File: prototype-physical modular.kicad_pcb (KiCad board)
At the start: 2 copper layers, 100 x 164 mm, 187 parts, among them CON1 BARREL_JACK, CON2 SD_Card, IC1 ATMEGA2560-A, P1 POWER, P10 PC, P11 CONN_UART, P12 PJ, P13 PD, P14 PE, P15 PH, P16 PF, P17 SD_PINS, P18 3VI2C, P19 PIGPIO, P2 FTDI, P20 MIDI_IN, P21 MIDI_OUT, P22 BUSTI, P23 BUSTO, P3 SPI, P7 PA, P8 PL, P9 PB, Q1 BSS138, Q2 BSS138, Q3 BSS138, Q4 BSS138, Q5 BSS138, Q6 BSS138, SW1 SW_PUSH, SW10 SW_PUSH, SW11 SW_PUSH, SW12 SW_PUSH, SW13 SW_PUSH, SW14 SW_PUSH, SW2 ROTARY_ENCODER_SWITCH, SW3 SW_PUSH, SW4 SW_PUSH, SW5 SW_PUSH, SW6 SW_PUSH, SW7 SW_PUSH, SW8 SW_PUSH, SW9 SW_PUSH, U1 NCP1117ST50T3G, U2 6N138, Y1 16MHz

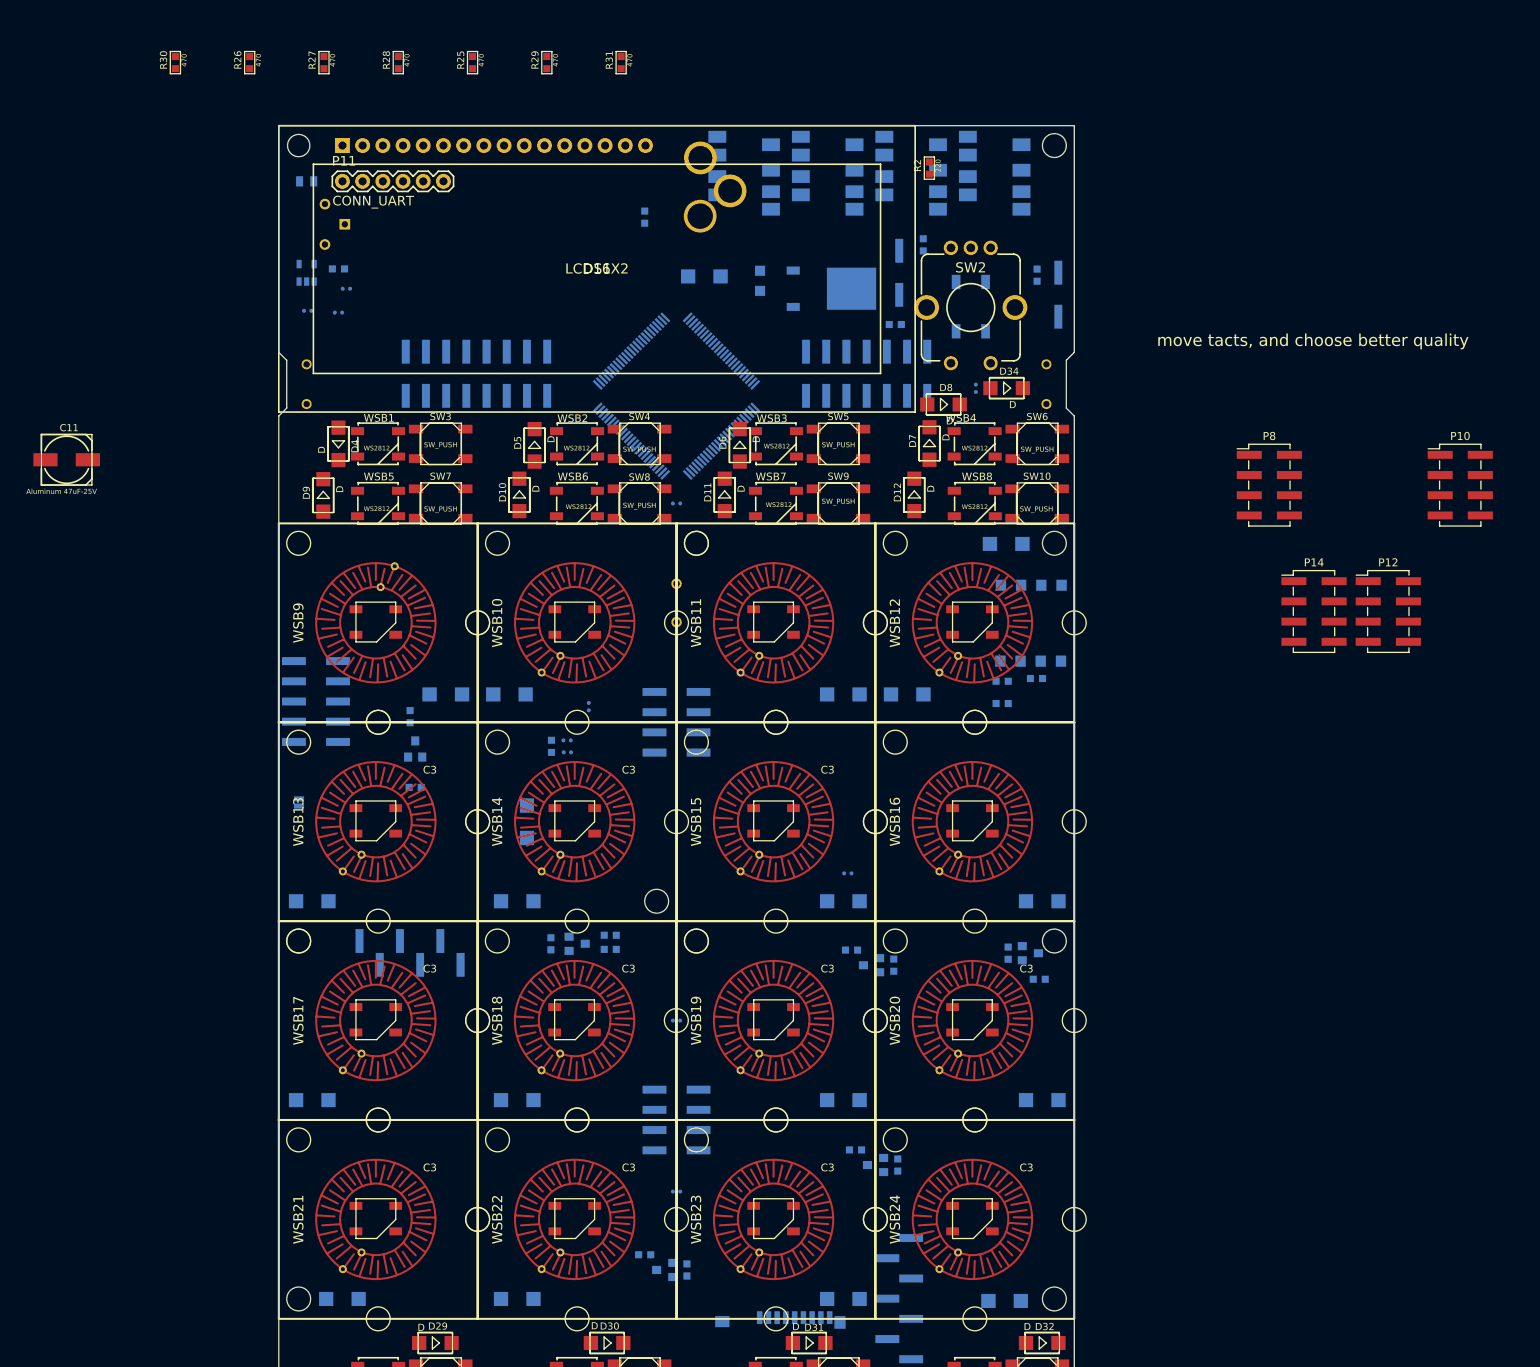
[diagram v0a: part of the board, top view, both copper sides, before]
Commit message: reflect schematic changes on board
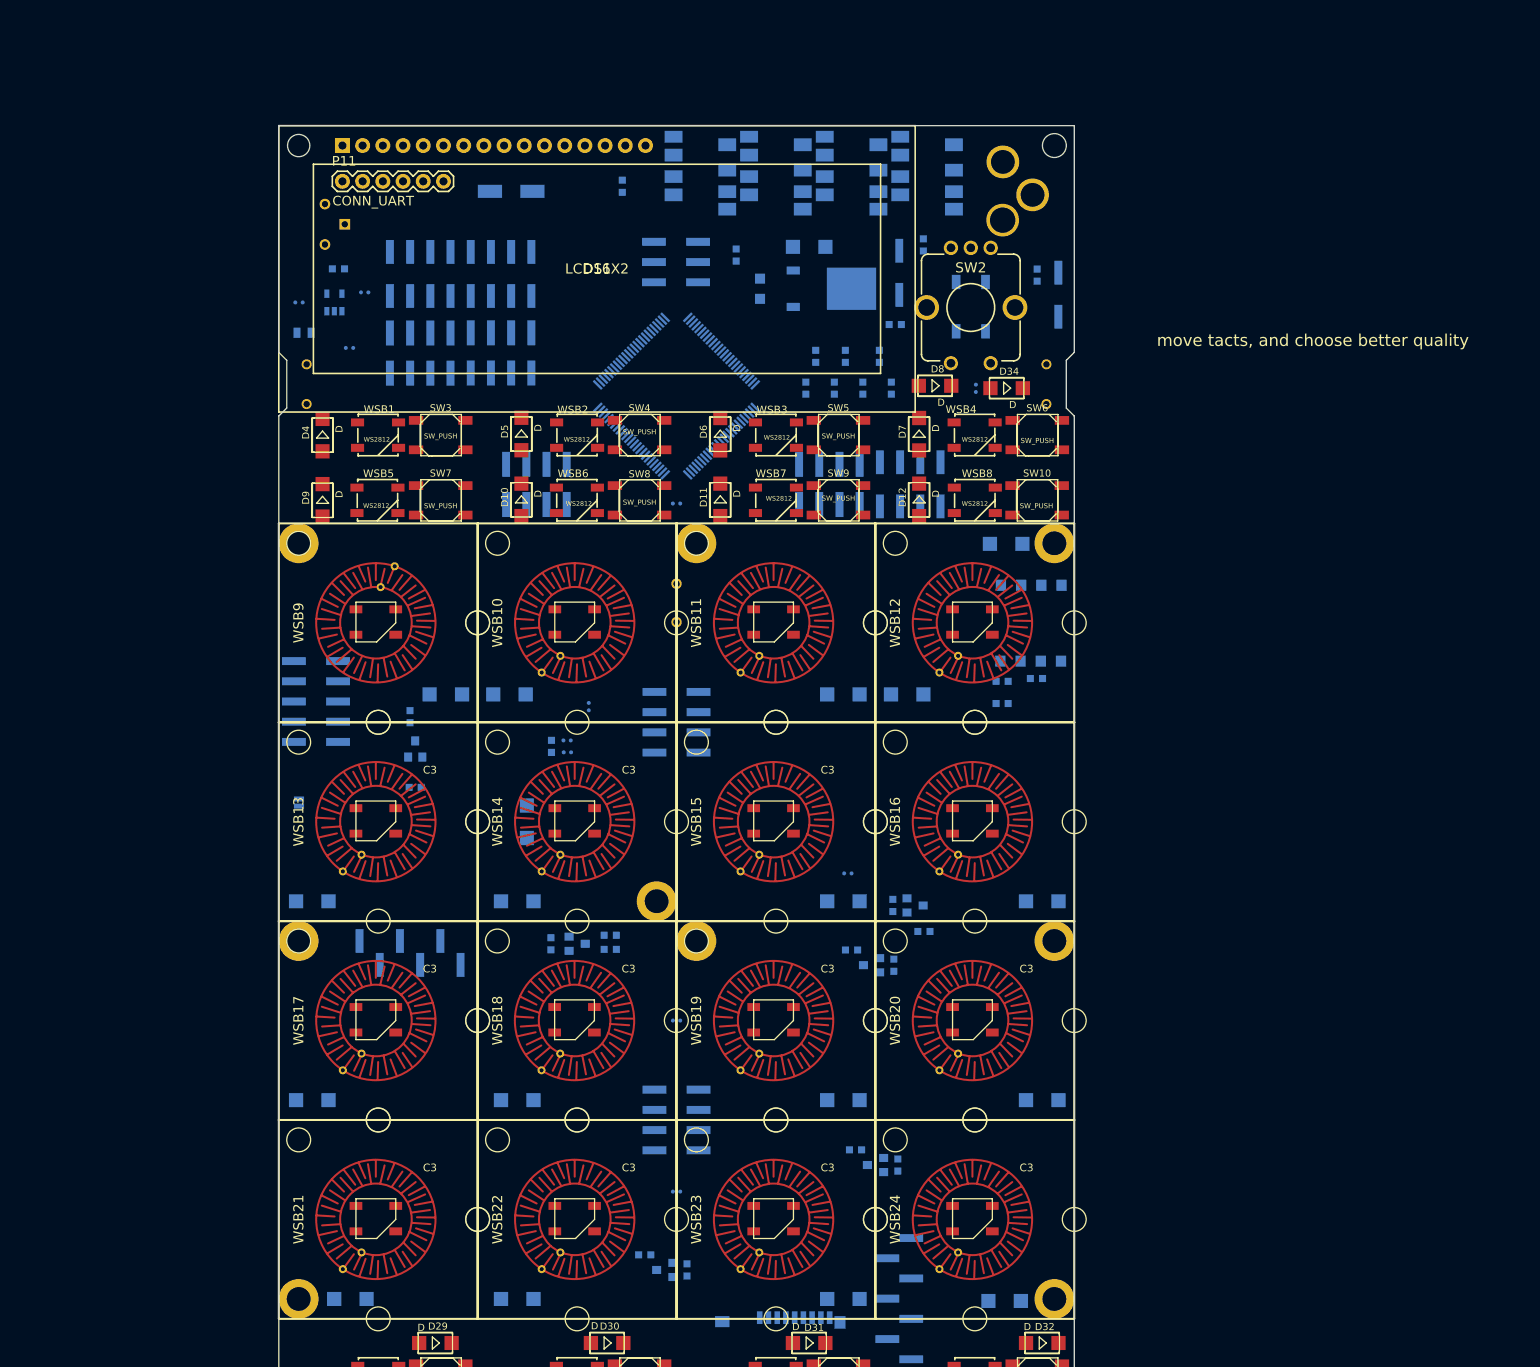
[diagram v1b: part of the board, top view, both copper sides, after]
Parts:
- C11, P10, P12, P14, P8, R2, R25, R26, R27, R28, R29, R30, R31: moved to B.Cu
- moved P12 126.0 mm to (17.8, 28.6), turned to 90 degrees
- moved P10 121.7 mm to (27.9, 28.6), turned to 90 degrees
- moved R30 98.9 mm to (77.0, 33.0), turned to 180 degrees
- moved P8 92.1 mm to (32.4, 45.1), turned to 270 degrees
- moved R26 87.3 mm to (73.4, 33.0), turned to 180 degrees
- moved R27 76.1 mm to (69.8, 33.0), turned to 180 degrees
- moved R28 65.6 mm to (66.3, 33.0), turned to 180 degrees
- moved C11 65.3 mm to (29.2, 8.26)
- moved R25 63.1 mm to (75.5, 29.0)
- moved P14 63.0 mm to (69.2, 45.1), turned to 90 degrees
- moved R29 52.6 mm to (71.2, 29.0), turned to 180 degrees
- moved R31 44.3 mm to (67.5, 29.0), turned to 180 degrees
- moved CON1 38.0 mm to (91.0, -2.00)
- moved P3 32.3 mm to (49.9, 17.1), turned to 0 degrees
- moved R2 26.6 mm to (57.5, 16.3)
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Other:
- board text added: "AUTOTEL calculator 20.10.2017"
- board text removed: "error: keep clear of tracks where there are nuts!"

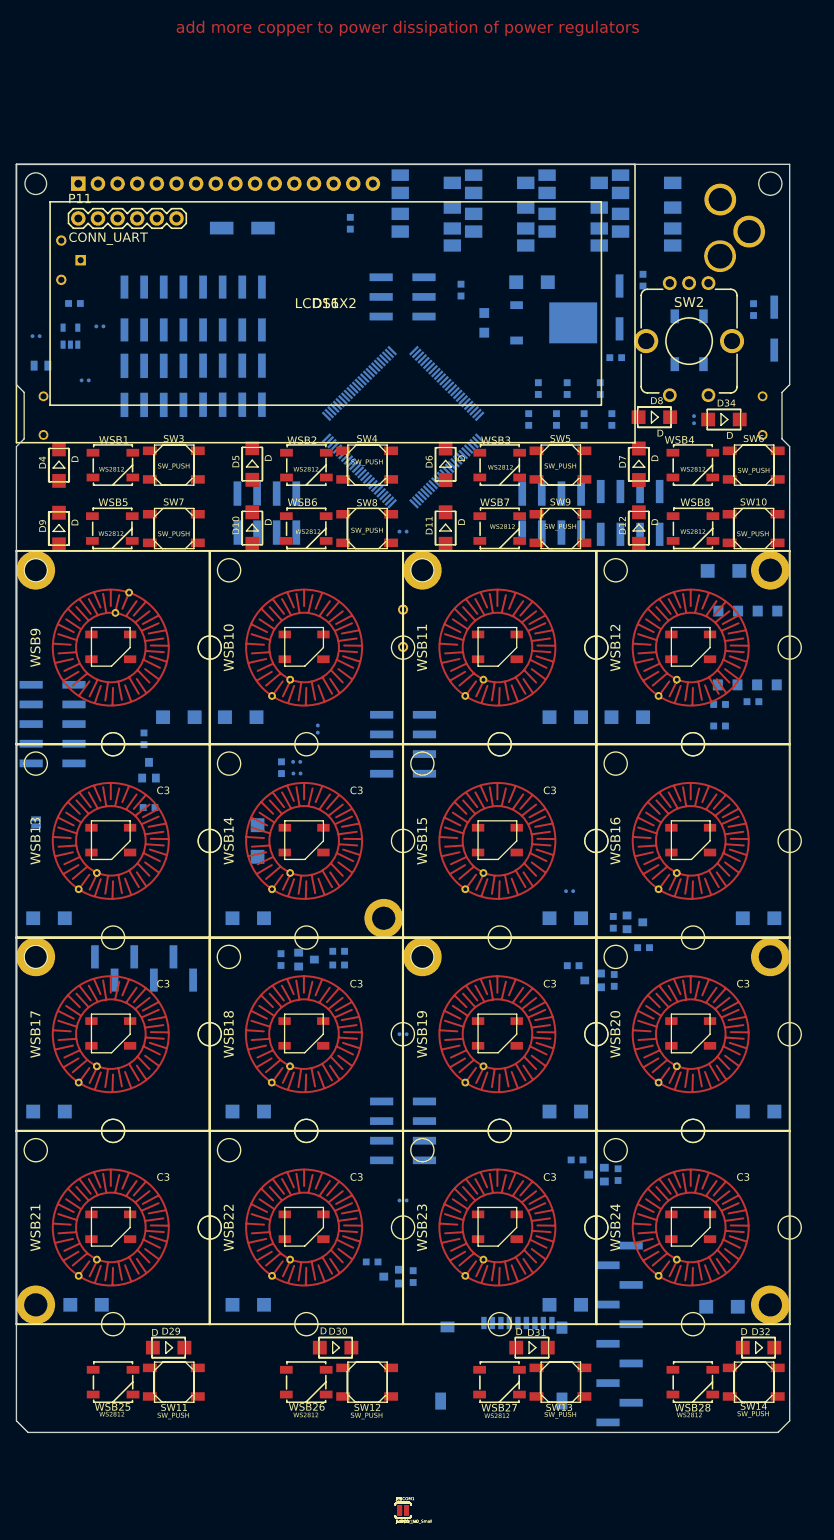
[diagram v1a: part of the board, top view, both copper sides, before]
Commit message: button matrix diodes needed to be inverse
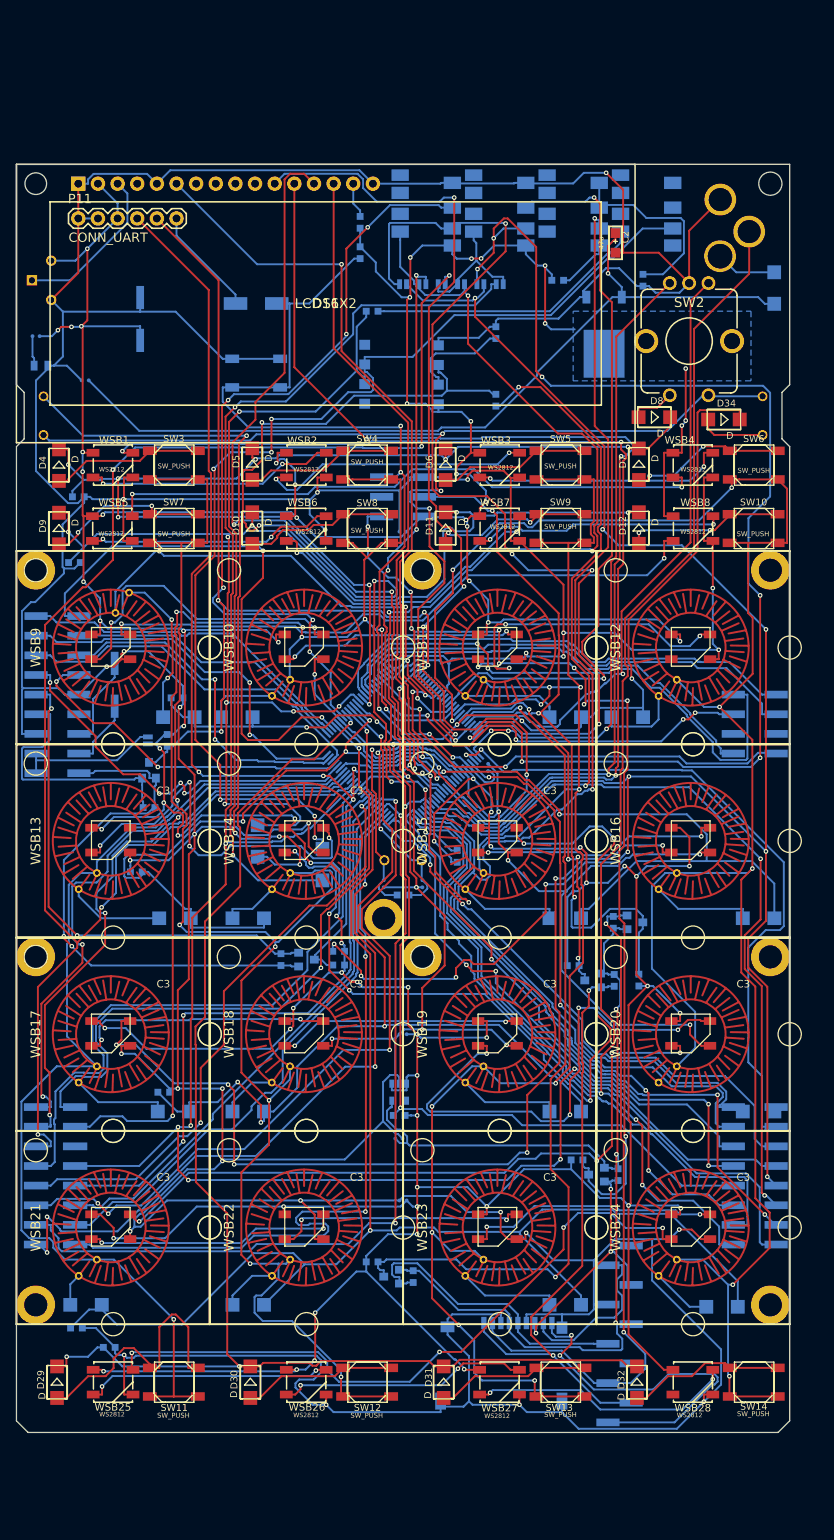
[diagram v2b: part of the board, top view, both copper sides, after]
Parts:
- removed P14: PE, Pin_Headers:Pin_Header_Straight_2x04_Pitch2.54mm_SMD
- removed P2: FTDI, Pin_Headers:Pin_Header_Straight_1x06_Pitch2.54mm_SMD_Pin1Left
- removed P8: PL, Pin_Headers:Pin_Header_Straight_2x04_Pitch2.54mm_SMD
- removed P9: PB, Pin_Headers:Pin_Header_Straight_2x04_Pitch2.54mm_SMD
- C2: moved to F.Cu
- JP1, JP3, JP4, JP5, PJ1COM1, PJ2COM1: moved to B.Cu
- moved PJ1COM1 159.1 mm to (62.5, 15.5), turned to 180 degrees
- moved JP5 158.9 mm to (60.0, 15.5), turned to 180 degrees
- moved JP1 158.8 mm to (57.5, 15.5), turned to 180 degrees
- moved PJ2COM1 158.7 mm to (55.0, 15.5)
- moved JP3 158.6 mm to (52.5, 15.5), turned to 180 degrees
- moved JP4 158.6 mm to (50.0, 15.5), turned to 180 degrees
- moved R30 136.4 mm to (7.76, 150.5), turned to 270 degrees
- moved R31 135.9 mm to (12.0, 153.0), turned to 270 degrees
- moved P15 132.3 mm to (95.5, 125.7), turned to 180 degrees
- moved R10 113.1 mm to (49.5, 123.0), turned to 90 degrees
- moved C3 111.9 mm to (49.5, 126.0), turned to 270 degrees
- moved P10 109.7 mm to (5.07, 135.9), turned to 0 degrees
- moved 3v3regu1 106.6 mm to (49.5, 120.0), turned to 270 degrees
- moved R29 104.9 mm to (19.1, 120.0), turned to 270 degrees
- moved P12 98.0 mm to (5.07, 125.7), turned to 180 degrees
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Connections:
- D10 pad +: /MUXBX1 -> Net-(D10-Pad+)
- D10 pad -: Net-(D10-Pad-) -> /MUXBX1
- D11 pad +: /MUXBX1 -> Net-(D11-Pad+)
- D11 pad -: Net-(D11-Pad-) -> /MUXBX1
- D12 pad +: /MUXBX1 -> Net-(D12-Pad+)
- D12 pad -: Net-(D12-Pad-) -> /MUXBX1
- D13 pad +: /MUXBX2 -> Net-(D13-Pad+)
- D13 pad -: Net-(D13-Pad-) -> /MUXBX2
- D14 pad +: /MUXBX2 -> Net-(D14-Pad+)
- D14 pad -: Net-(D14-Pad-) -> /MUXBX2
- D15 pad +: /MUXBX2 -> Net-(D15-Pad+)
- D15 pad -: Net-(D15-Pad-) -> /MUXBX2
- D16 pad +: /MUXBX2 -> Net-(D16-Pad+)
- D16 pad -: Net-(D16-Pad-) -> /MUXBX2
- D17 pad +: /MUXBX3 -> Net-(D17-Pad+)
- D17 pad -: Net-(D17-Pad-) -> /MUXBX3
- D18 pad +: /MUXBX3 -> Net-(D18-Pad+)
- D18 pad -: Net-(D18-Pad-) -> /MUXBX3
- D19 pad +: /MUXBX3 -> Net-(D19-Pad+)
- D19 pad -: Net-(D19-Pad-) -> /MUXBX3
- D20 pad +: /MUXBX3 -> Net-(D20-Pad+)
- D20 pad -: Net-(D20-Pad-) -> /MUXBX3
- D21 pad +: /MUXBX4 -> Net-(D21-Pad+)
- D21 pad -: Net-(D21-Pad-) -> /MUXBX4
- D22 pad +: /MUXBX4 -> Net-(D22-Pad+)
- D22 pad -: Net-(D22-Pad-) -> /MUXBX4
- D23 pad +: /MUXBX4 -> Net-(D23-Pad+)
- D23 pad -: Net-(D23-Pad-) -> /MUXBX4
- D24 pad +: /MUXBX4 -> Net-(D24-Pad+)
- D24 pad -: Net-(D24-Pad-) -> /MUXBX4
- D25 pad +: /MUXBX5 -> Net-(D25-Pad+)
- D25 pad -: Net-(D25-Pad-) -> /MUXBX5
- D26 pad +: /MUXBX5 -> Net-(D26-Pad+)
- D26 pad -: Net-(D26-Pad-) -> /MUXBX5
- D27 pad +: /MUXBX5 -> Net-(D27-Pad+)
- D27 pad -: Net-(D27-Pad-) -> /MUXBX5
- D28 pad +: /MUXBX5 -> Net-(D28-Pad+)
- D28 pad -: Net-(D28-Pad-) -> /MUXBX5
- D29 pad +: /MUXBX6 -> Net-(D29-Pad+)
- D29 pad -: Net-(D29-Pad-) -> /MUXBX6
- D30 pad +: /MUXBX6 -> Net-(D30-Pad+)
- D30 pad -: Net-(D30-Pad-) -> /MUXBX6
- D31 pad +: /MUXBX6 -> Net-(D31-Pad+)
- D31 pad -: Net-(D31-Pad-) -> /MUXBX6
- D32 pad +: /MUXBX6 -> Net-(D32-Pad+)
- D32 pad -: Net-(D32-Pad-) -> /MUXBX6
- D33 pad +: /MUXBX1 -> Net-(D33-Pad+)
- D33 pad -: Net-(D33-Pad-) -> /MUXBX1
- D34 pad +: /MUXBX2 -> Net-(D34-Pad+)
- D34 pad -: Net-(D34-Pad-) -> /MUXBX2
- D4 pad +: /MUXBX0 -> Net-(D4-Pad+)
- D4 pad -: Net-(D4-Pad-) -> /MUXBX0
- D5 pad +: /MUXBX0 -> Net-(D5-Pad+)
- D5 pad -: Net-(D5-Pad-) -> /MUXBX0
- D6 pad +: /MUXBX0 -> Net-(D6-Pad+)
- D6 pad -: Net-(D6-Pad-) -> /MUXBX0
- D7 pad +: /MUXBX0 -> Net-(D7-Pad+)
- D7 pad -: Net-(D7-Pad-) -> /MUXBX0
- D8 pad +: /MUXBX0 -> Net-(D8-Pad+)
- D8 pad -: Net-(D8-Pad-) -> /MUXBX0
- D9 pad +: /MUXBX1 -> Net-(D9-Pad+)
- D9 pad -: Net-(D9-Pad-) -> /MUXBX1
- SW10 pad 1: Net-(D12-Pad-) -> Net-(D12-Pad+)
- SW11 pad 1: Net-(D29-Pad-) -> Net-(D29-Pad+)
- SW12 pad 1: Net-(D30-Pad-) -> Net-(D30-Pad+)
- SW13 pad 1: Net-(D31-Pad-) -> Net-(D31-Pad+)
- SW14 pad 1: Net-(D32-Pad-) -> Net-(D32-Pad+)
- SW2 pad E: Net-(D8-Pad-) -> Net-(D8-Pad+)
- SW3 pad 1: Net-(D4-Pad-) -> Net-(D4-Pad+)
- SW4 pad 1: Net-(D5-Pad-) -> Net-(D5-Pad+)
- SW5 pad 1: Net-(D6-Pad-) -> Net-(D6-Pad+)
- SW6 pad 1: Net-(D7-Pad-) -> Net-(D7-Pad+)
- SW7 pad 1: Net-(D9-Pad-) -> Net-(D9-Pad+)
- SW8 pad 1: Net-(D10-Pad-) -> Net-(D10-Pad+)
- SW9 pad 1: Net-(D11-Pad-) -> Net-(D11-Pad+)
- SW_left1 pad 1: Net-(D33-Pad-) -> Net-(D33-Pad+)
- SW_right1 pad 1: Net-(D34-Pad-) -> Net-(D34-Pad+)
- WSB10 pad 5: Net-(D14-Pad-) -> Net-(D14-Pad+)
- WSB11 pad 5: Net-(D15-Pad-) -> Net-(D15-Pad+)
- WSB12 pad 5: Net-(D16-Pad-) -> Net-(D16-Pad+)
- WSB13 pad 5: Net-(D17-Pad-) -> Net-(D17-Pad+)
- WSB14 pad 5: Net-(D18-Pad-) -> Net-(D18-Pad+)
- WSB15 pad 5: Net-(D19-Pad-) -> Net-(D19-Pad+)
- WSB16 pad 5: Net-(D20-Pad-) -> Net-(D20-Pad+)
- WSB17 pad 5: Net-(D21-Pad-) -> Net-(D21-Pad+)
- WSB18 pad 5: Net-(D22-Pad-) -> Net-(D22-Pad+)
- WSB19 pad 5: Net-(D23-Pad-) -> Net-(D23-Pad+)
- WSB20 pad 5: Net-(D24-Pad-) -> Net-(D24-Pad+)
- WSB21 pad 5: Net-(D25-Pad-) -> Net-(D25-Pad+)
- WSB22 pad 5: Net-(D26-Pad-) -> Net-(D26-Pad+)
- WSB23 pad 5: Net-(D27-Pad-) -> Net-(D27-Pad+)
- WSB24 pad 5: Net-(D28-Pad-) -> Net-(D28-Pad+)
- WSB9 pad 5: Net-(D13-Pad-) -> Net-(D13-Pad+)
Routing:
- net GND: track 0.00 -> 1122.6 mm, vias 0 -> 39
- net +5V: track 0.00 -> 897.1 mm, vias 0 -> 80
- net /BUS_COM: track 0.00 -> 277.6 mm, vias 0 -> 7
- net /TX3: track 0.00 -> 275.9 mm, vias 0 -> 7
- net /MUXAX3: track 0.00 -> 267.8 mm, vias 0 -> 7
- net /SCL: track 0.00 -> 263.0 mm, vias 0 -> 11
- net /MUXAX1: track 0.00 -> 253.3 mm, vias 0 -> 11
- net /MUXAX0: track 0.00 -> 236.3 mm, vias 0 -> 5
- net /MUXAX2: track 0.00 -> 223.9 mm, vias 0 -> 9
- net Net-(IC1-Pad65): track 0.00 -> 212.5 mm, vias 0 -> 5
- net /POWER_IS: track 0.00 -> 202.4 mm, vias 0 -> 3
- net /MUXBX5: track 0.00 -> 194.4 mm, vias 0 -> 2
- net /MIDI_OUT_TX: track 0.00 -> 180.3 mm, vias 0 -> 4
- net /MUXBX6: track 0.00 -> 176.7 mm, vias 0 -> 3
- net /MUXBX1: track 0.00 -> 172.4 mm, vias 0 -> 9
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- added copper zone on B.Cu, net +5V
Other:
- board text added: "AUTOTEL.CO calculator 20.10.2017"
- board text removed: "AUTOTEL calculator 20.10.2017"
- board text removed: "add more copper to power dissipation of power regulators"
